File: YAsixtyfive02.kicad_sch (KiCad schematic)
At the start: 25 parts, among them J1 ~{NMI}, U1 WD65C02, U10 74LS138, U2 ROM 28C256, U3 RAM 62256, U4 74HCT00, U5 74LS30, U7 74HCT273, U9 MC6850_

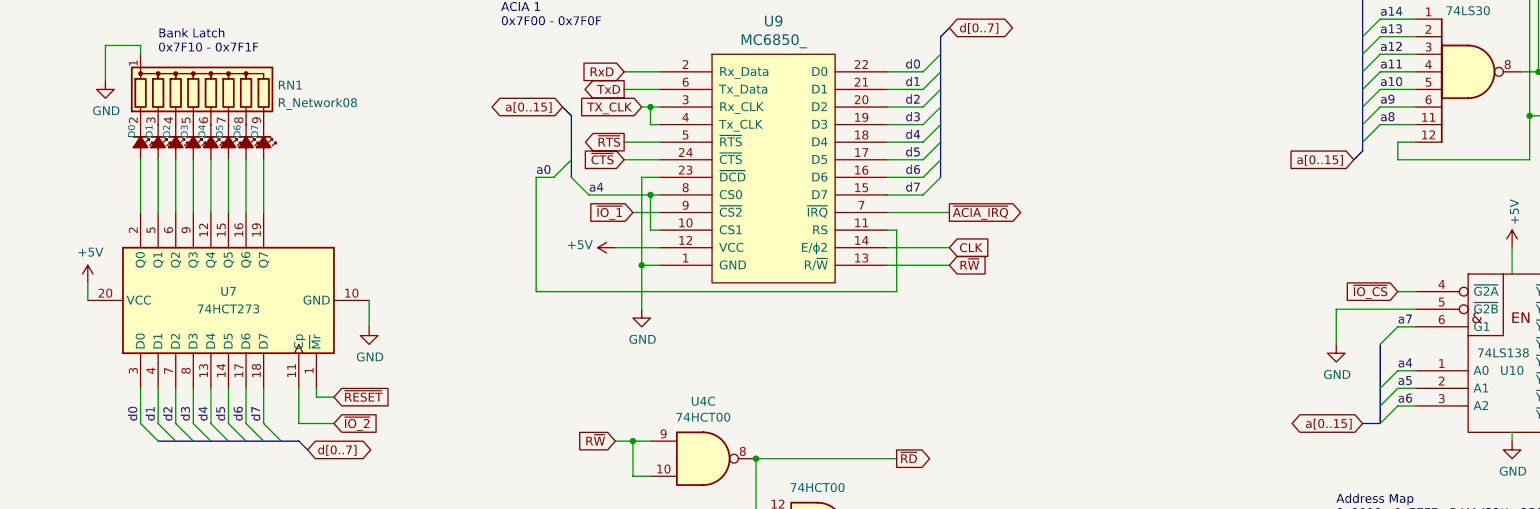
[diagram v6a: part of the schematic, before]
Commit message: 6502 Bus Edge Connector done
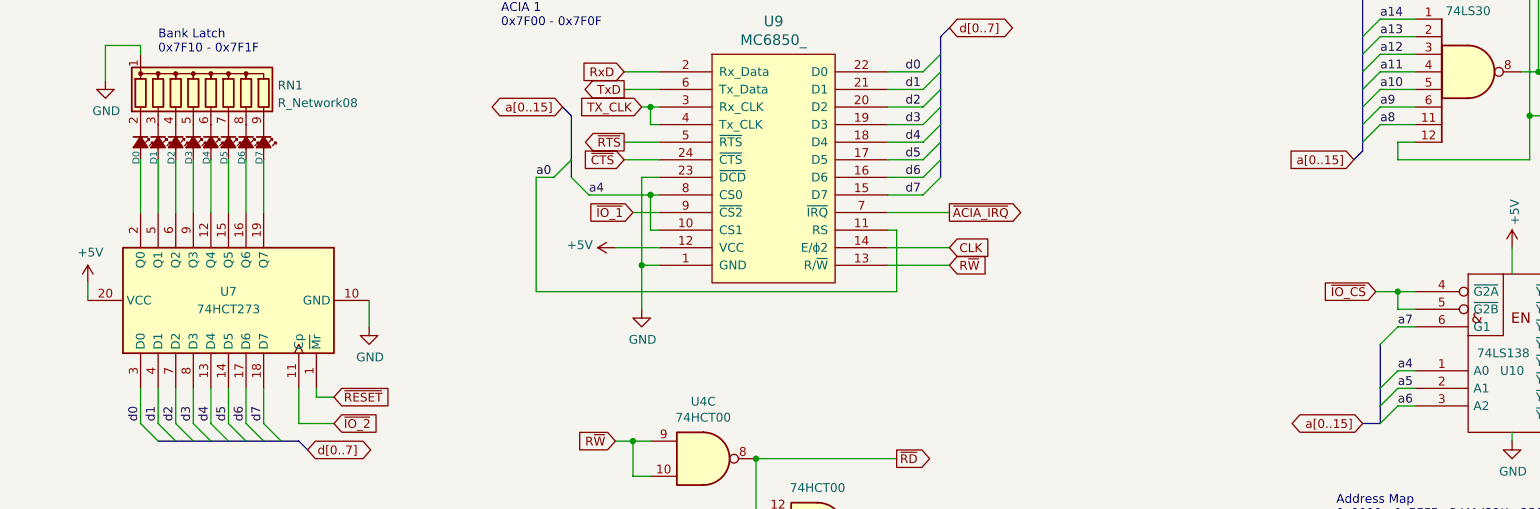
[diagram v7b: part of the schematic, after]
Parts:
- D0, D1, D2, D3, D4, D5, D6, D7: footprint LED_THT:LED_D3.0mm -> LED_THT:LED_SMALL_3.0mm
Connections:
- net GND: no longer U10.5 (~{G2B})
- net ~{IO_CS}: now also U10.5 (~{G2B})
